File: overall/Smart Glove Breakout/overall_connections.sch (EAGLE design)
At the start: 15 parts, among them IC1 LD1085

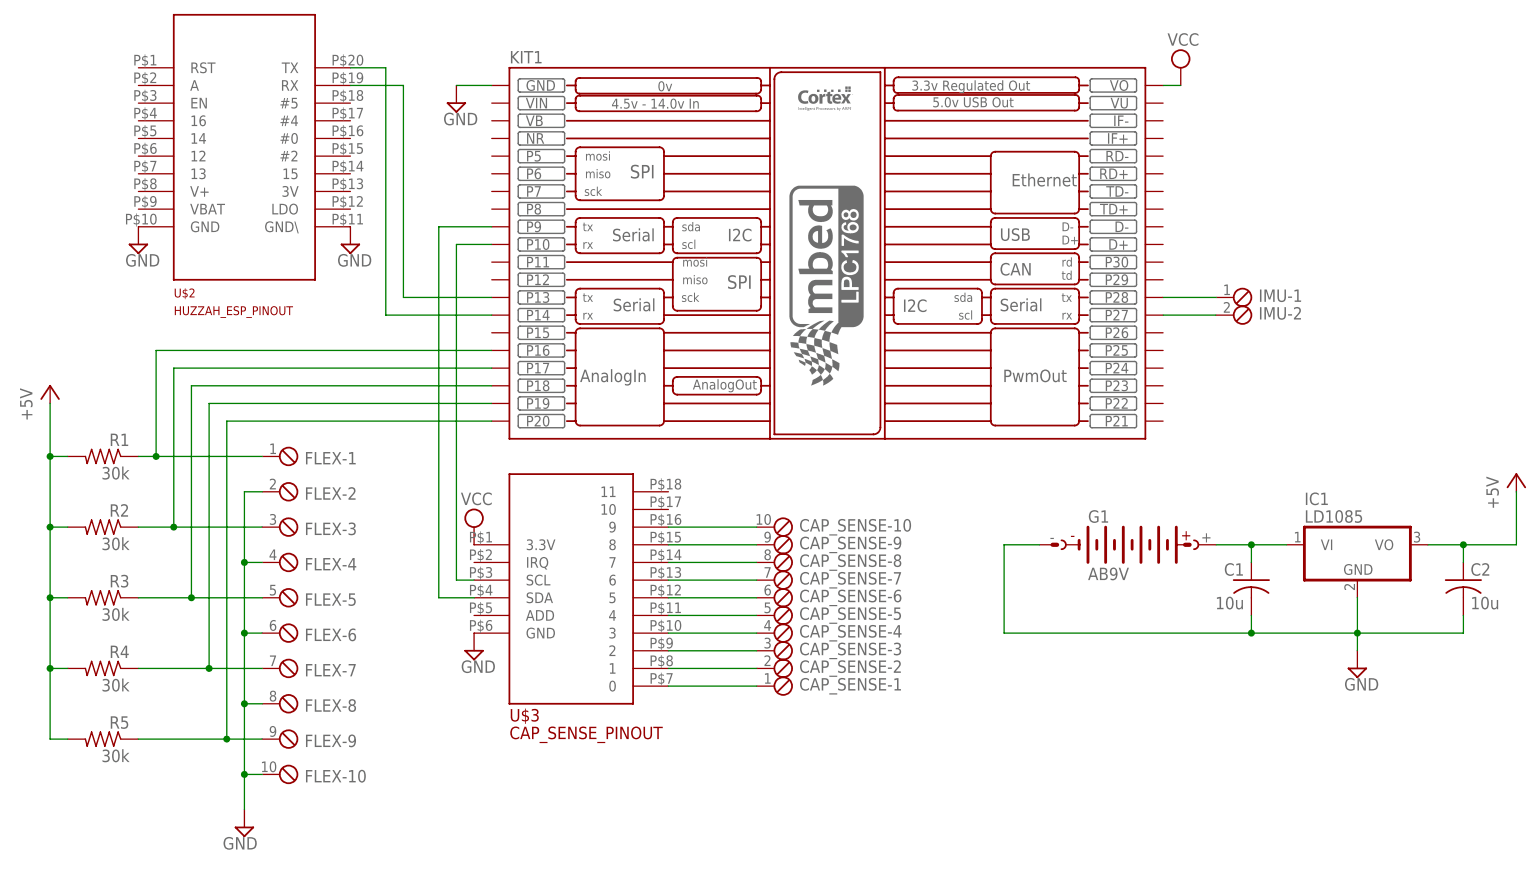
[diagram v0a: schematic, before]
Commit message: Revised PCB design
Fixed error with voltage regulator pinout, package pins for our device
did not match the Eagle schematic. Also routed V+ pins to both the mbed
device and the Huzzah IC.
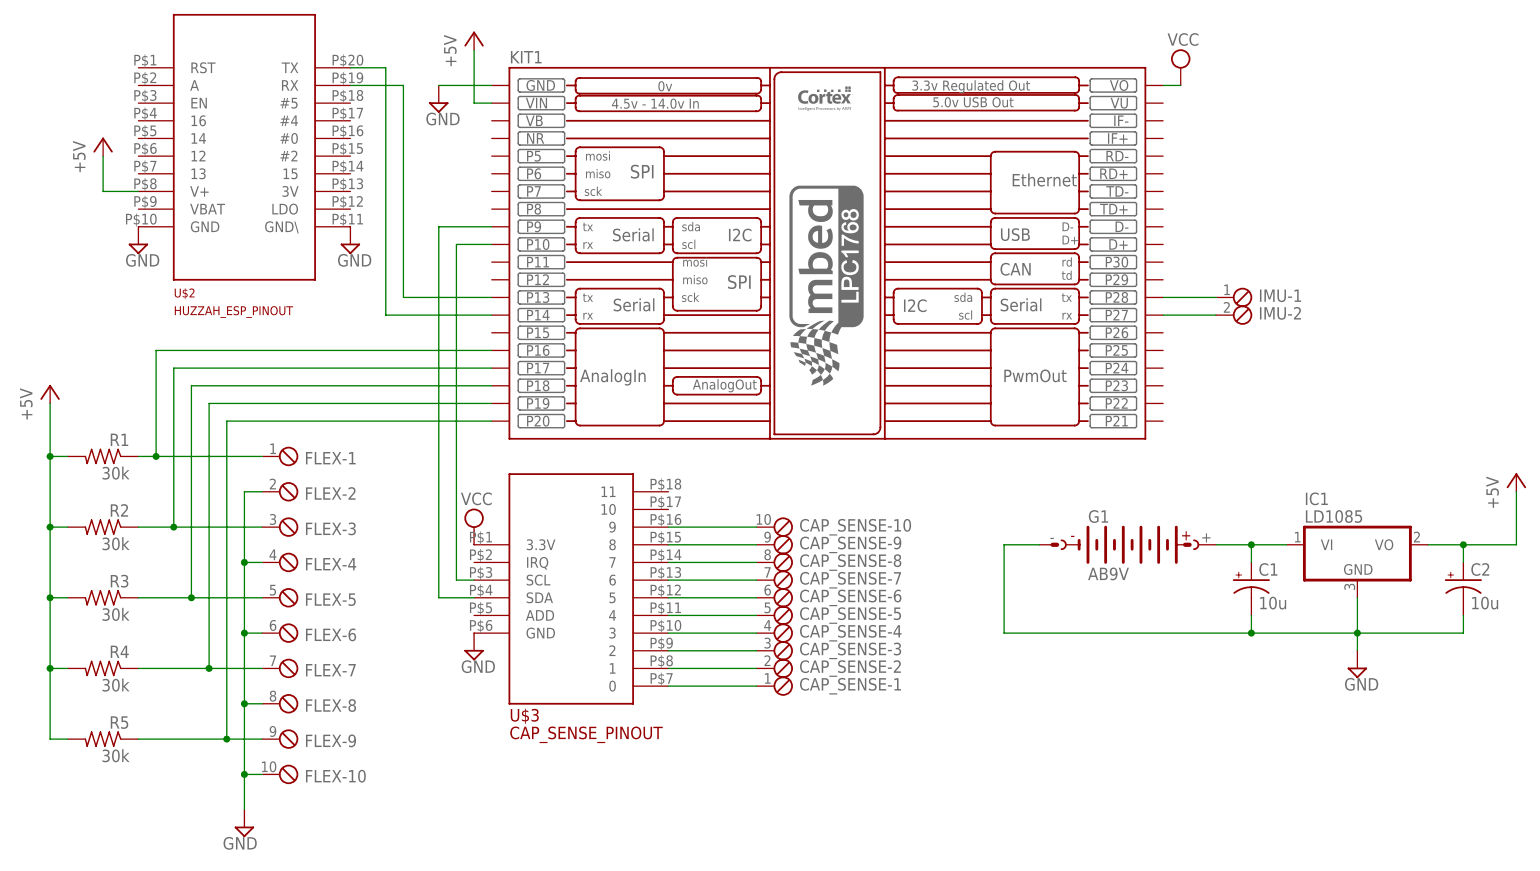
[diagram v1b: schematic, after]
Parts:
- C1, C2: device rcl:C-USC1206 -> rcl:CPOL-USE1.8-4
- IC1: device linear:7805T -> smart_glove_breakout:7805T
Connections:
- net +5V: now also C2.+, KIT1.VIN, U$2.V+; no longer C2.1
- net GND: now also C1.-, C2.-; no longer C1.2, C2.2
- net N$10: now also C1.+; no longer C1.1
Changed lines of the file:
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@@
 <part name="R5" library="resistor" deviceset="R-US_" device="0204/7" value="30k"/>
 <part name="P+1" library="supply1" deviceset="+5V" device=""/>
-<part name="IC1" library="linear" deviceset="78*" device="T" technology="05" value="LD1085"/>
 <part name="SUPPLY8" library="supply2" deviceset="GND" device=""/>
 <part name="G1" library="battery" deviceset="AB9V" device=""/>
 <part name="P+2" library="supply1" deviceset="+5V" device=""/>
-<part name="C1" library="rcl" deviceset="C-US" device="C1206" value="10u"/>
-<part name="C2" library="rcl" deviceset="C-US" device="C1206" value="10u"/>
 <part name="IMU" library="con-phoenix-254" deviceset="MPT2" device=""/>
+<part name="C1" library="rcl" deviceset="CPOL-US" device="E1.8-4" value="10u"/>
+<part name="C2" library="rcl" deviceset="CPOL-US" device="E1.8-4" value="10u"/>
+<part name="IC1" library="smart_glove_breakout" deviceset="78*" device="T" technology="05" value="LD1085"/>
+<part name="P+3" library="supply1" deviceset="+5V" device=""/>
+<part name="P+4" library="supply1" deviceset="+5V" device=""/>
 </parts>
 <sheets>
@@
 <instance part="U$3" gate="G$1" x="-38.1" y="-60.96"/>
 <instance part="KIT1" gate="KIT" x="7.62" y="-25.4"/>
-<instance part="SUPPLY1" gate="GND" x="-45.72" y="-5.08"/>
+<instance part="SUPPLY1" gate="GND" x="-48.26" y="-5.08"/>
 <instance part="SUPPLY2" gate="GND" x="-43.18" y="-83.82"/>
 <instance part="SUPPLY3" gate="GND" x="-91.44" y="-25.4"/>
@@
 <instance part="R5" gate="G$1" x="-96.52" y="-96.52" rot="MR0"/>
 <instance part="P+1" gate="1" x="-104.14" y="-45.72"/>
-<instance part="IC1" gate="A1" x="83.82" y="-68.58"/>
 <instance part="SUPPLY8" gate="GND" x="83.82" y="-86.36"/>
 <instance part="G1" gate="G$1" x="50.8" y="-68.58"/>
 <instance part="P+2" gate="1" x="106.68" y="-58.42"/>
-<instance part="C1" gate="G$1" x="68.58" y="-73.66" rot="MR0"/>
-<instance part="C2" gate="G$1" x="99.06" y="-73.66"/>
 <instance part="IMU" gate="-1" x="66.04" y="-33.02"/>
 <instance part="IMU" gate="-2" x="66.04" y="-35.56"/>
+<instance part="C1" gate="G$1" x="68.58" y="-73.66"/>
+<instance part="C2" gate="G$1" x="99.06" y="-73.66"/>
+<instance part="IC1" gate="A1" x="83.82" y="-68.58"/>
+<instance part="P+3" gate="1" x="-96.52" y="-10.16"/>
+<instance part="P+4" gate="1" x="-43.18" y="5.08"/>
 </instances>
 <busses>
@@
 <pinref part="KIT1" gate="KIT" pin="GND"/>
 <pinref part="SUPPLY1" gate="GND" pin="GND"/>
-<wire x1="-40.64" y1="-2.54" x2="-45.72" y2="-2.54" width="0.1524" layer="91"/>
+<wire x1="-40.64" y1="-2.54" x2="-48.26" y2="-2.54" width="0.1524" layer="91"/>
 </segment>
 <segment>
@@
 <pinref part="SUPPLY8" gate="GND" pin="GND"/>
 <wire x1="83.82" y1="-81.28" x2="83.82" y2="-83.82" width="0.1524" layer="91"/>
-<pinref part="IC1" gate="A1" pin="GND"/>
-<wire x1="83.82" y1="-76.2" x2="83.82" y2="-81.28" width="0.1524" layer="91"/>
 <junction x="83.82" y="-81.28"/>
 <wire x1="99.06" y1="-78.74" x2="99.06" y2="-81.28" width="0.1524" layer="91"/>
@@
 <wire x1="33.02" y1="-81.28" x2="68.58" y2="-81.28" width="0.1524" layer="91"/>
 <junction x="68.58" y="-81.28"/>
-<pinref part="C1" gate="G$1" pin="2"/>
-<pinref part="C2" gate="G$1" pin="2"/>
+<pinref part="C1" gate="G$1" pin="-"/>
+<pinref part="C2" gate="G$1" pin="-"/>
+<pinref part="IC1" gate="A1" pin="GND"/>
+<wire x1="83.82" y1="-76.2" x2="83.82" y2="-81.28" width="0.1524" layer="91"/>
 </segment>
 </net>
@@
 <pinref part="P+2" gate="1" pin="+5V"/>
 <wire x1="106.68" y1="-60.96" x2="106.68" y2="-68.58" width="0.1524" layer="91"/>
-<pinref part="IC1" gate="A1" pin="VO"/>
 <wire x1="93.98" y1="-68.58" x2="99.06" y2="-68.58" width="0.1524" layer="91"/>
 <wire x1="99.06" y1="-68.58" x2="99.06" y2="-71.12" width="0.1524" layer="91"/>
 <wire x1="106.68" y1="-68.58" x2="99.06" y2="-68.58" width="0.1524" layer="91"/>
 <junction x="99.06" y="-68.58"/>
-<pinref part="C2" gate="G$1" pin="1"/>
+<pinref part="C2" gate="G$1" pin="+"/>
+<pinref part="IC1" gate="A1" pin="VO"/>
+</segment>
+<segment>
+<pinref part="U$2" gate="G$1" pin="V+"/>
+<pinref part="P+3" gate="1" pin="+5V"/>
+<wire x1="-91.44" y1="-17.78" x2="-96.52" y2="-17.78" width="0.1524" layer="91"/>
+<wire x1="-96.52" y1="-17.78" x2="-96.52" y2="-12.7" width="0.1524" layer="91"/>
+</segment>
+<segment>
+<pinref part="KIT1" gate="KIT" pin="VIN"/>
+<pinref part="P+4" gate="1" pin="+5V"/>
+<wire x1="-40.64" y1="-5.08" x2="-43.18" y2="-5.08" width="0.1524" layer="91"/>
+<wire x1="-43.18" y1="-5.08" x2="-43.18" y2="2.54" width="0.1524" layer="91"/>
 </segment>
 </net>
@@
 <segment>
 <wire x1="68.58" y1="-71.12" x2="68.58" y2="-68.58" width="0.1524" layer="91"/>
-<pinref part="IC1" gate="A1" pin="VI"/>
 <wire x1="68.58" y1="-68.58" x2="73.66" y2="-68.58" width="0.1524" layer="91"/>
 <pinref part="G1" gate="G$1" pin="+"/>
 <wire x1="63.5" y1="-68.58" x2="68.58" y2="-68.58" width="0.1524" layer="91"/>
 <junction x="68.58" y="-68.58"/>
-<pinref part="C1" gate="G$1" pin="1"/>
-</segment>
-</net>
+<pinref part="C1" gate="G$1" pin="+"/>
+<pinref part="IC1" gate="A1" pin="VI"/>
+</segment>
+</net>
